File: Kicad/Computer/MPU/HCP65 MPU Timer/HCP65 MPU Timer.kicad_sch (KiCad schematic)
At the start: 20 parts, among them IC1 74LVC2G74DP,125, IC11 74LVC1G27GW,125, IC14 74HCT4040PW,118, IC2 74LVC273PW,118, IC5 AP7365-33WG-7, IC6 74HCT4040PW,118, IC7 PI3B3251QE, IC9 74LVC541APW,118, J1 Pin_Header_01x16, J2 Conn_02x16_Counter_Clockwise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

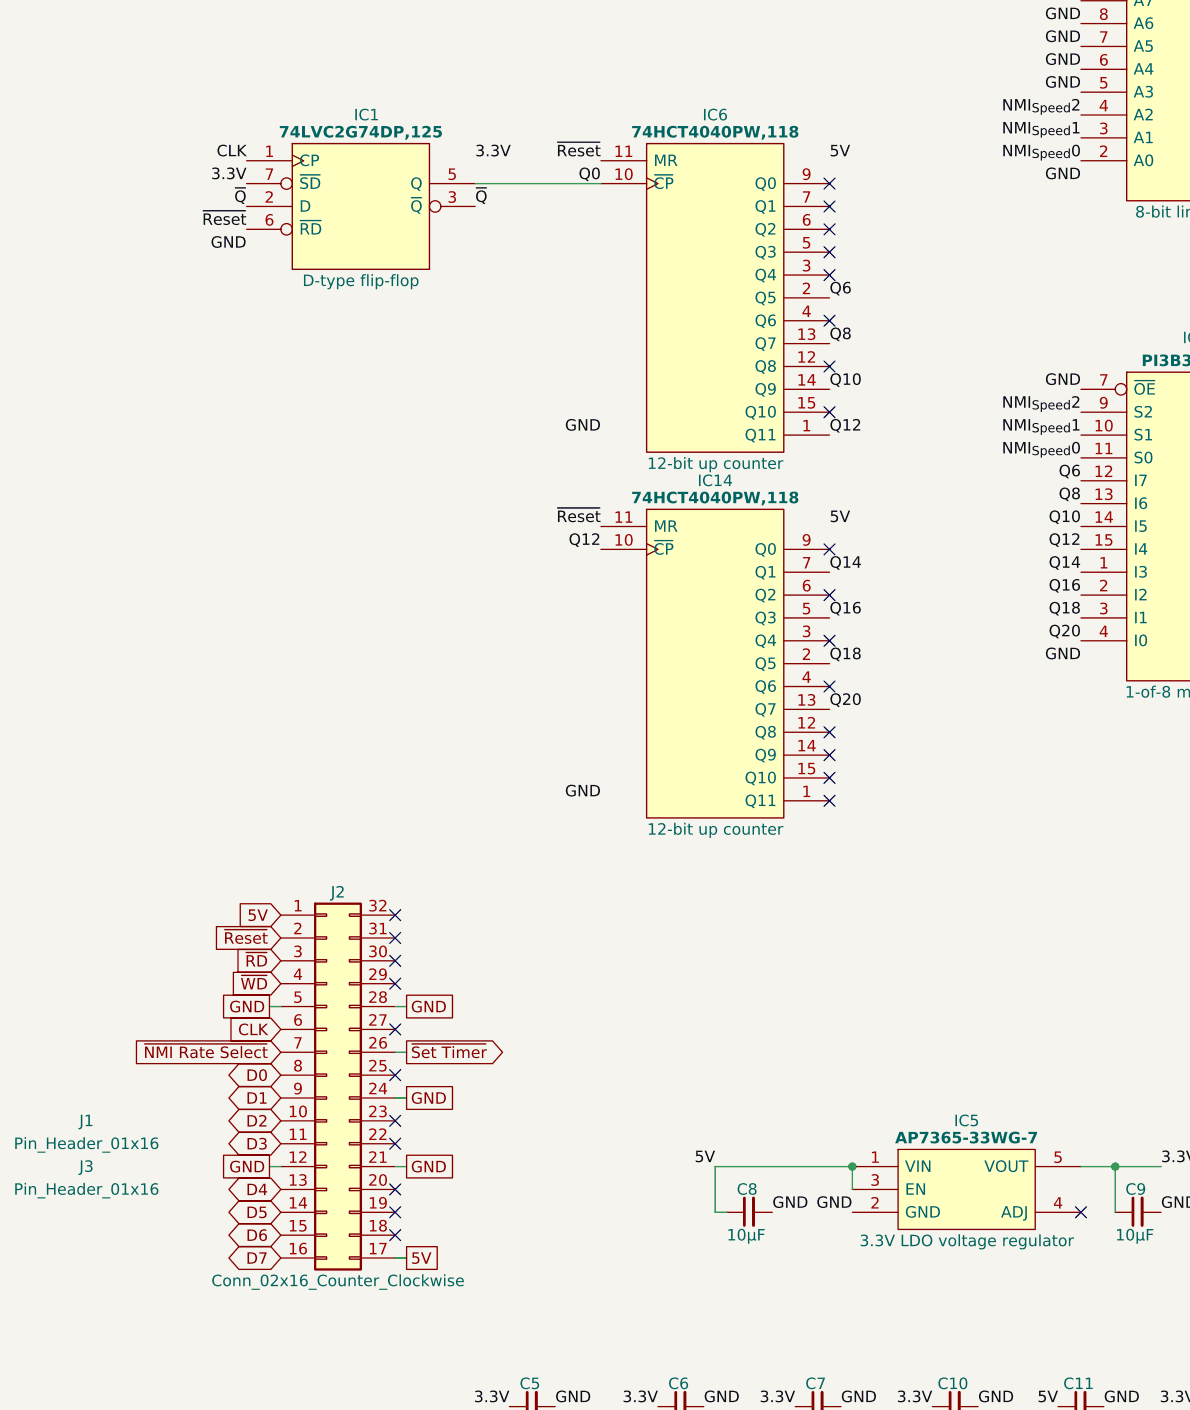
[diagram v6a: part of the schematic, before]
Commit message: Added a (potentially) 50MHz board.
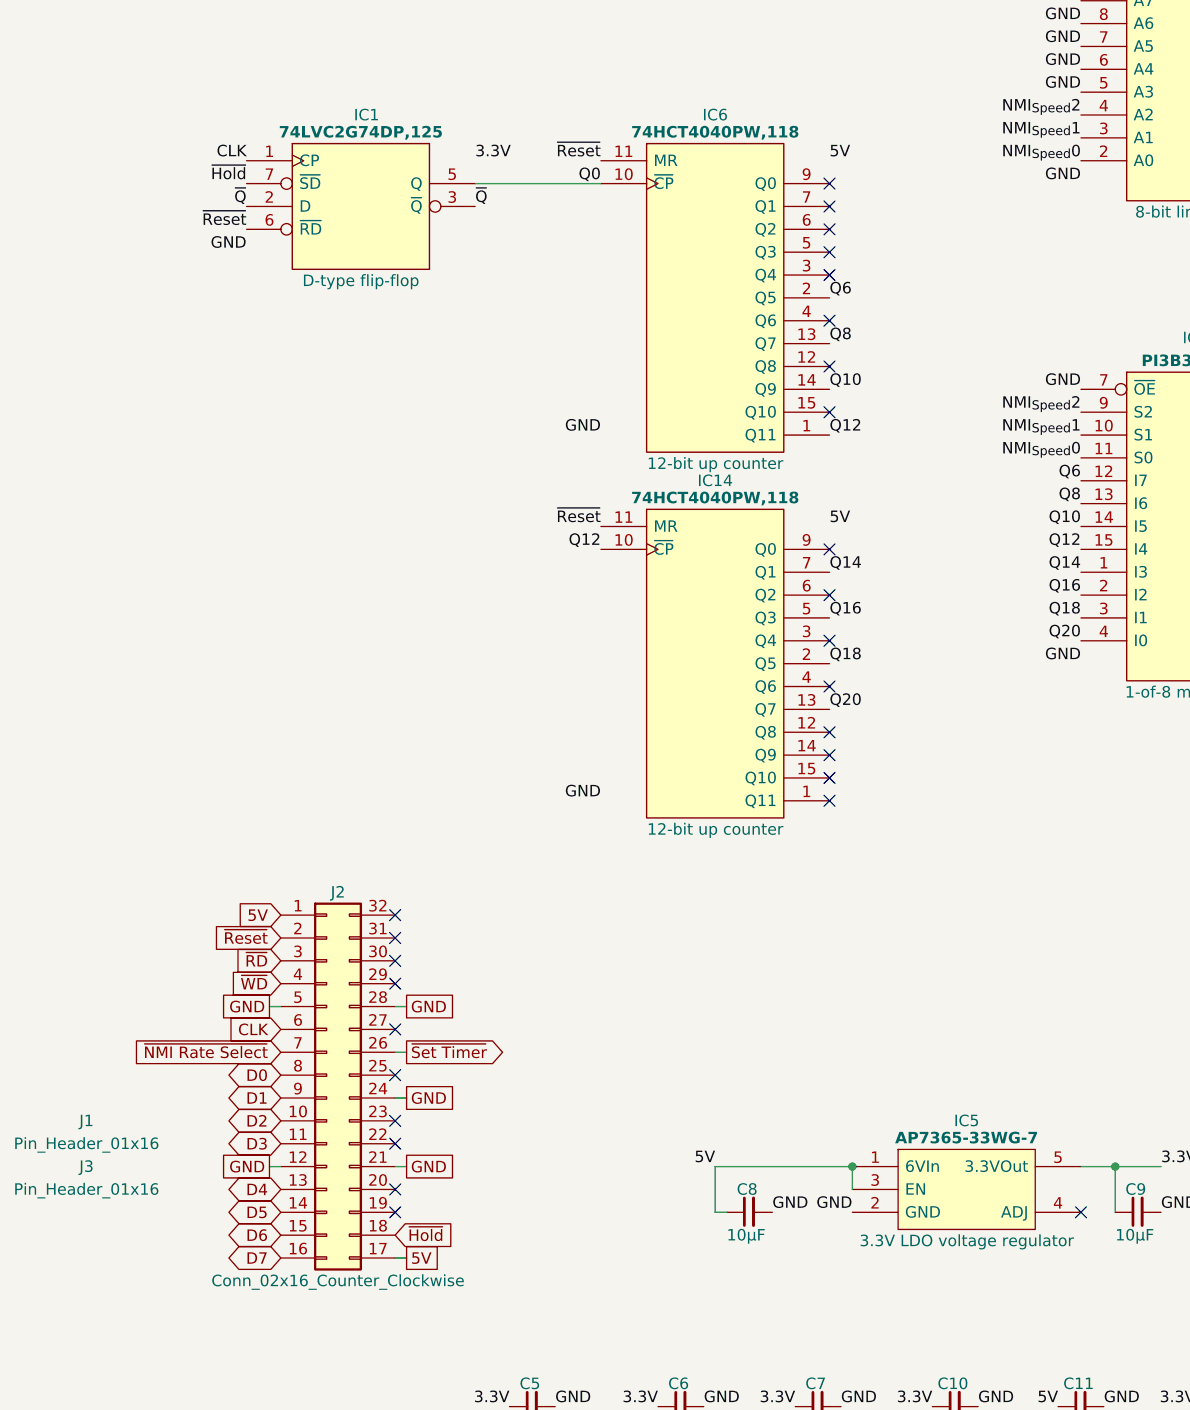
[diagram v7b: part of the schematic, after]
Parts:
- C10, C11, C15, C16, C5, C6, C7, C8, C9: Garbage Unpolarized capacitor, small symbol -> (none)
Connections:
- net 3.3V: no longer IC1.7 (~{SD})
- net ~{Hold}: now reaches J2.18 (Pin_18)
- net ~{Hold}: now also IC1.7 (~{SD})
- no-connect marks 33 -> 32
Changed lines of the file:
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@@
 	)
 	(no_connect
-		(at 64.77 165.1)
-	)
-	(no_connect
 		(at 113.03 58.42)
 	)
@@
 		)
 	)
-	(label "3.3V"
-		(at 48.26 48.26 180)
-		(fields_autoplaced yes)
-		(effects
-			(font
-				(size 1.27 1.27)
-			)
-			(justify right bottom)
-		)
-	)
 	(label "D4"
 		(at 166.37 35.56 0)
@@
 		)
 	)
+	(label "~{Hold}"
+		(at 48.26 48.26 180)
+		(fields_autoplaced yes)
+		(effects
+			(font
+				(size 1.27 1.27)
+			)
+			(justify right bottom)
+		)
+	)
 	(label "GND"
 		(at 114.3 184.15 0)
@@
 		)
 	)
+	(global_label "~{Hold}"
+		(shape input)
+		(at 64.77 165.1 0)
+		(fields_autoplaced yes)
+		(effects
+			(font
+				(size 1.27 1.27)
+			)
+			(justify left)
+		)
+		(property "Intersheetrefs" "${INTERSHEET_REFS}"
+			(at 72.0489 165.1 0)
+			(effects
+				(font
+					(size 1.27 1.27)
+				)
+				(justify left)
+				(hide yes)
+			)
+		)
+	)
 	(global_label "5V"
 		(shape passive)
@@
 			)
 		)
-		(property "Garbage" "Unpolarized capacitor, small symbol"
-			(at 109.22 184.15 0)
-			(effects
-				(font
-					(size 1.27 1.27)
-				)
-				(hide yes)
-			)
-		)
 		(pin "1"
 		)
@@
 			)
 		)
-		(property "Garbage" "Unpolarized capacitor, small symbol"
-			(at 93.98 184.15 0)
-			(effects
-				(font
-					(size 1.27 1.27)
-				)
-				(hide yes)
-			)
-		)
 		(pin "1"
 		)
@@
 			)
 		)
-		(property "Garbage" "Unpolarized capacitor, small symbol"
-			(at 101.6 162.56 0)
-			(effects
-				(font
-					(size 1.27 1.27)
-				)
-				(hide yes)
-			)
-		)
 		(pin "1"
 		)
@@
 					(unit 1)
 				)
-				(path "/5ce90b85-49a2-4937-86c7-662b0d6f8431/662feba9-2017-4e89-b774-f7d895f327d7"
-					(reference "C19")
-					(unit 1)
-				)
 				(path "/5ce90b85-49a2-4937-86c7-662b0d6f8431/435bbe75-130b-4ff1-a245-161bf90dff48"
 					(reference "C7")
 					(unit 1)
 				)
+				(path "/5ce90b85-49a2-4937-86c7-662b0d6f8431/662feba9-2017-4e89-b774-f7d895f327d7"
+					(reference "C19")
+					(unit 1)
+				)
 			)
 			(project "Sound"
@@
 			)
 		)
-		(property "Garbage" "Unpolarized capacitor, small symbol"
-			(at 167.64 184.15 0)
-			(effects
-				(font
-					(size 1.27 1.27)
-				)
-				(hide yes)
-			)
-		)
 		(pin "1"
 		)
@@
 					(unit 1)
 				)
-				(path "/5ce90b85-49a2-4937-86c7-662b0d6f8431/662feba9-2017-4e89-b774-f7d895f327d7"
-					(reference "IC6")
-					(unit 1)
-				)
 				(path "/5ce90b85-49a2-4937-86c7-662b0d6f8431/435bbe75-130b-4ff1-a245-161bf90dff48"
 					(reference "IC24")
 					(unit 1)
 				)
+				(path "/5ce90b85-49a2-4937-86c7-662b0d6f8431/662feba9-2017-4e89-b774-f7d895f327d7"
+					(reference "IC6")
+					(unit 1)
+				)
 			)
 			(project "Sound"
@@
 			)
 		)
-		(property "Garbage" "Unpolarized capacitor, small symbol"
-			(at 144.78 162.56 0)
-			(effects
-				(font
-					(size 1.27 1.27)
-				)
-				(hide yes)
-			)
-		)
 		(pin "1"
 		)
@@
 					(unit 1)
 				)
-				(path "/5ce90b85-49a2-4937-86c7-662b0d6f8431/662feba9-2017-4e89-b774-f7d895f327d7"
-					(reference "C20")
-					(unit 1)
-				)
 				(path "/5ce90b85-49a2-4937-86c7-662b0d6f8431/435bbe75-130b-4ff1-a245-161bf90dff48"
 					(reference "C8")
 					(unit 1)
 				)
+				(path "/5ce90b85-49a2-4937-86c7-662b0d6f8431/662feba9-2017-4e89-b774-f7d895f327d7"
+					(reference "C20")
+					(unit 1)
+				)
 			)
 			(project "Sound"
@@
 			)
 		)
-		(property "Garbage" "Unpolarized capacitor, small symbol"
-			(at 138.43 184.15 0)
-			(effects
-				(font
-					(size 1.27 1.27)
-				)
-				(hide yes)
-			)
-		)
 		(pin "1"
 		)
@@
 			)
 		)
-		(property "Garbage" "Unpolarized capacitor, small symbol"
-			(at 77.47 184.15 0)
-			(effects
-				(font
-					(size 1.27 1.27)
-				)
-				(hide yes)
-			)
-		)
 		(pin "1"
 		)
@@
 			)
 		)
-		(property "Garbage" "Unpolarized capacitor, small symbol"
-			(at 153.67 184.15 0)
-			(effects
-				(font
-					(size 1.27 1.27)
-				)
-				(hide yes)
-			)
-		)
 		(pin "1"
 		)
@@
 			(at 124.46 184.15 0)
 			(effects
-				(font
-					(size 1.27 1.27)
-				)
-				(hide yes)
-			)
-		)
-		(property "Garbage" "Unpolarized capacitor, small symbol"
-			(at 124.46 184.15 0)
-			(effects

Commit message: Panelised Speed Board.
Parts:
- IC5: Garbage DiodesZetex AP7365-33WG-7, LDO Voltage Regulator, 600mA, 3.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 -> (none)
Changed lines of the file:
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@@
-			)
-		)
-		(property "Garbage" "DiodesZetex AP7365-33WG-7, LDO Voltage Regulator, 600mA, 3.3 V +/-2%, 2  6 Vin, 5-Pin SOT-25"
-			(at 137.16 195.072 0)
-			(effects
-				(font
-					(size 1.27 1.27)
-				)
-				(justify left)
-				(hide yes)
 			)
 		)
